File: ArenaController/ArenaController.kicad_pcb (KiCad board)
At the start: 2 copper layers, 63 x 112.3 mm, 30 parts, among them J1 RJ45, J2 RJ45, J4 RJ45, J5 RJ45, J6 RJ45, J7 Barrel_Jack, J8 Screw_Terminal_01x04, Q1 FS3400, Q2 FS3400, Q3 FS3400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

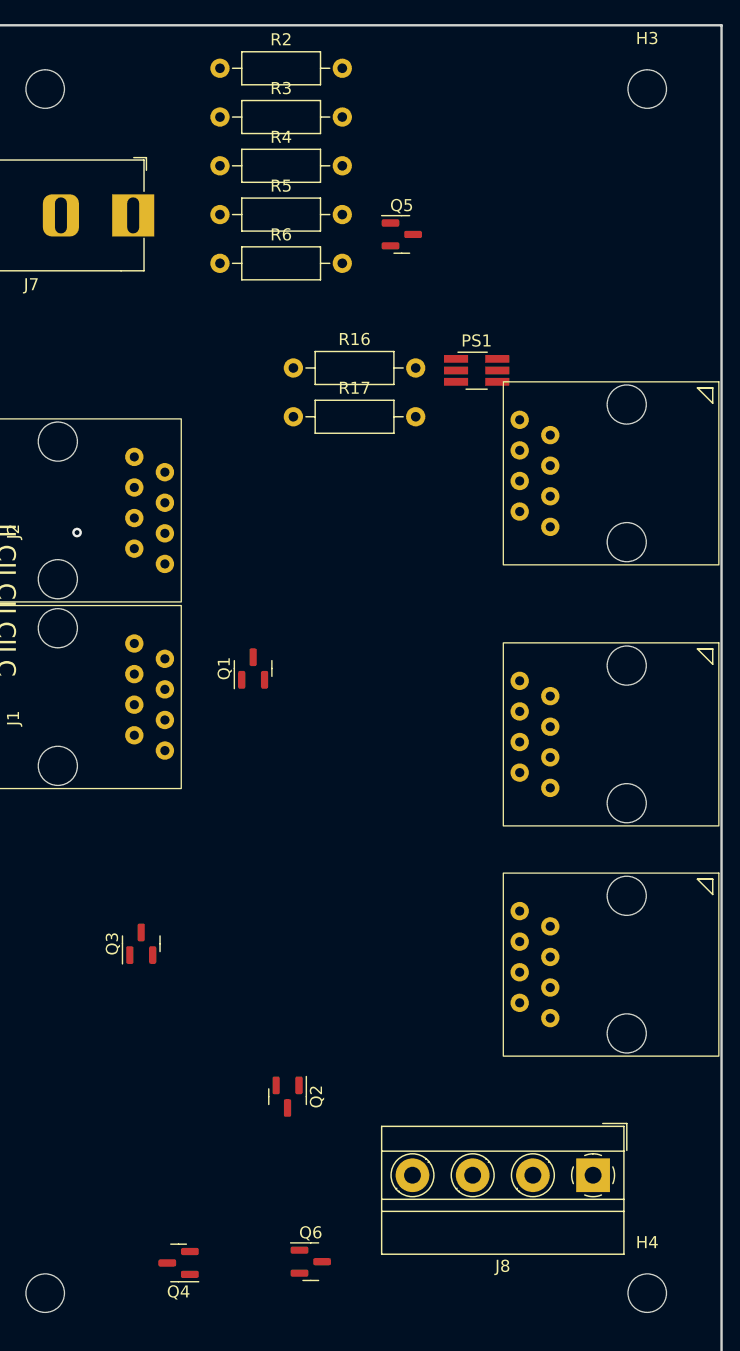
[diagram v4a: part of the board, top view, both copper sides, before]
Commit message: Added more SMD nightmare parts.
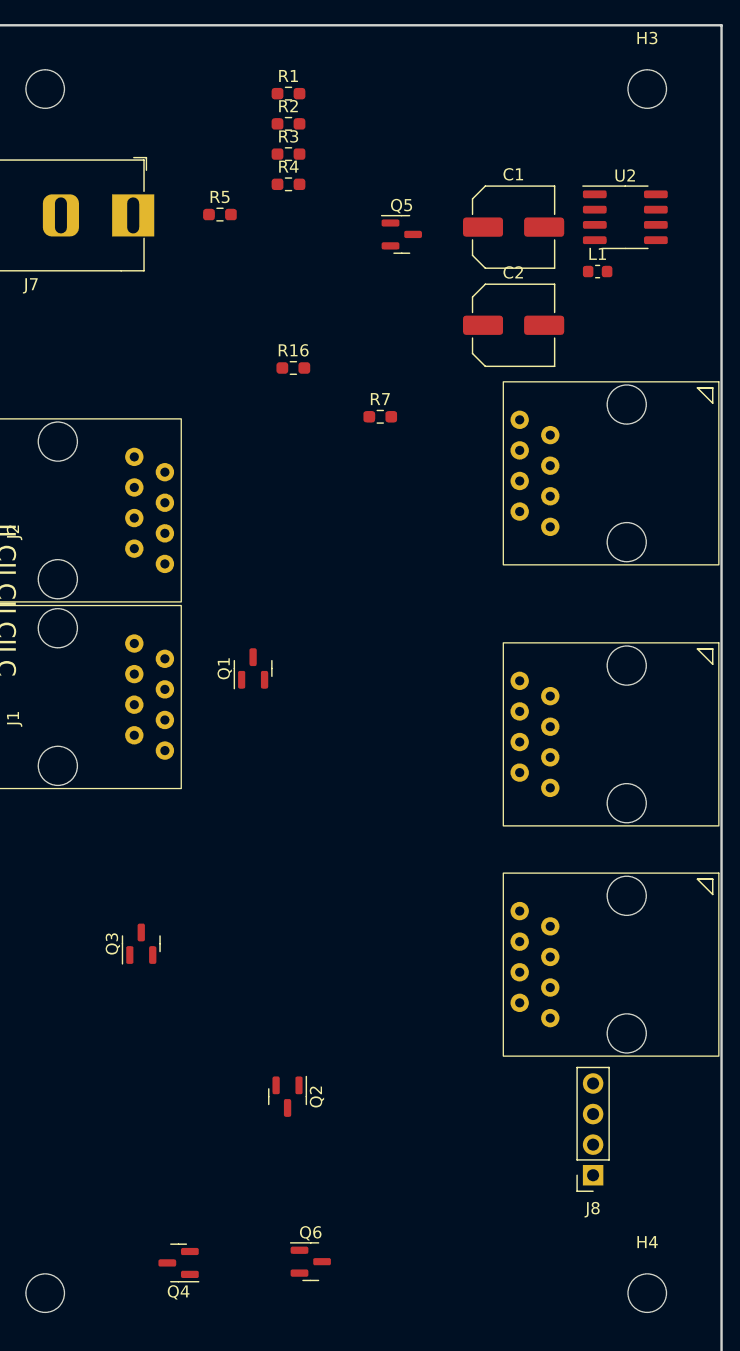
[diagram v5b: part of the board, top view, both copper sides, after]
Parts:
- removed PS1: ~, Package_TO_SOT_SMD:TSOT-23-6_HandSoldering
- removed R17: 10k, Resistor_THT:R_Axial_DIN0207_L6.3mm_D2.5mm_P10.16mm_Horizontal
- removed R6: 330, Resistor_THT:R_Axial_DIN0207_L6.3mm_D2.5mm_P10.16mm_Horizontal
- added C1: 100uF, Capacitor_SMD:C_Elec_6.3x5.4, F.Cu at (88.9, 61.5)
- added C2: 470uF, Capacitor_SMD:C_Elec_6.3x7.7, F.Cu at (88.9, 69.6)
- added L1: 47uH, Inductor_SMD:L_0603_1608Metric, F.Cu at (95.9, 65.2)
- added R1: 330, Resistor_SMD:R_0603_1608Metric_Pad0.98x0.95mm_HandSolder, F.Cu at (70.2, 50.4)
- added R7: 10k, Resistor_SMD:R_0603_1608Metric_Pad0.98x0.95mm_HandSolder, F.Cu at (77.8, 77.2)
- added U2: ~, Package_SO:SOP-8_3.76x4.96mm_P1.27mm, F.Cu at (98.2, 60.6)
- J8: footprint TerminalBlock_MetzConnect:TerminalBlock_MetzConnect_Type011_RT05504HBWC_1x04_P5.00mm_Horizontal -> Connector_PinSocket_2.54mm:PinSocket_1x04_P2.54mm_Vertical
- R16, R2, R3, R4, R5: footprint Resistor_THT:R_Axial_DIN0207_L6.3mm_D2.5mm_P10.16mm_Horizontal -> Resistor_SMD:R_0603_1608Metric_Pad0.98x0.95mm_HandSolder
- moved R2 7.33 mm to (70.2, 52.9)
- moved R3 6.47 mm to (70.2, 55.4)
- moved R4 5.90 mm to (70.2, 57.9)
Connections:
- R2 pad 1: Net-(Q1-G) -> Net-(Q3-G)
- R2 pad 2: /m_Green -> /m_Horn
- R3 pad 1: Net-(Q2-G) -> Net-(Q5-G)
- R3 pad 2: /m_Red_1 -> /m_Red_2
- R4 pad 1: Net-(Q3-G) -> Net-(Q2-G)
- R4 pad 2: /m_Horn -> /m_Red_1
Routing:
- net GND: vias 1 -> 0

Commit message: Swapped to ESP32 Devkit 4.
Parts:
- removed J7: Barrel_Jack, footprints:BarrelJack_Horizontal_TwoPin
- added J9: Barrel_Jack_MountingPin, Connector_BarrelJack:BarrelJack_Horizontal, F.Cu at (57.4, 64.5)
- added U3: ESP32-Devkit_C_V4, footprints:MODULE_ESP32_DEVKIT_C_V4, F.Cu at (19.3, 77.7)
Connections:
- L1 pad 1: Net-(U2-SW) -> Net-(L1-Pad1)
- U2 pad 5: (no net) -> Net-(L1-Pad1)
- U2 pad 6: (no net) -> Net-(L1-Pad1)
- U2 pad 7: (no net) -> GND
- U2 pad 8: (no net) -> GND

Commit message: small boardwork cleanup to try and lay it out.
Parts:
- removed kibuzzard-638A2138: G***, kibuzzard-638A2138
- removed kibuzzard-638A214B: G***, kibuzzard-638A214B
- removed kibuzzard-638A2165: G***, kibuzzard-638A2165
- removed kibuzzard-638A2178: G***, kibuzzard-638A2178
- moved J1 143.1 mm to (180.6, 67.2), turned to -90 degrees
- moved R1 72.4 mm to (131.2, 89.4)
- moved R2 72.4 mm to (131.2, 91.9)
- moved R3 72.4 mm to (131.2, 94.4)
- moved R4 72.4 mm to (131.2, 96.9)
- moved J4 61.5 mm to (122.8, 155.2), turned to 180 degrees
- moved Q4 60.6 mm to (115.8, 121.4)
- moved J9 53.1 mm to (110.2, 58.8), turned to -90 degrees
- moved L1 52.9 mm to (148.2, 57.5)
- moved R16 52.9 mm to (122.9, 65.5)
- moved Q3 52.9 mm to (110.3, 113.4)
- moved J6 52.9 mm to (158.3, 66.7)
- moved J8 52.9 mm to (147.8, 132.6)
- moved Q1 52.9 mm to (119.6, 90.5)
- moved Q2 52.9 mm to (122.5, 126.1)
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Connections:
- J4 pad 5: /G_Pause -> unconnected-(J4-Pad5)
- J4 pad 6: /G_End -> unconnected-(J4-Pad6)
- J4 pad 7: /G_Reset -> /G_End
- U2 pad 2: (no net) -> unconnected-(U2-NC-Pad2)
- U3 pad 11: /G_Reset -> unconnected-(U3-GPIO18/V_SPI_CLK/SCK-Pad11)
- U3 pad 25: /G_Pause -> unconnected-(U3-RTC_GPIO5/ADC1_7/GPIO35-Pad25)
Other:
- board size 63 x 112.3 mm -> 60 x 110 mm
- board text added: "Button 1"
- board text added: "Button 2"
- board text added: "Stacklight 1"
- board text added: "Stacklight 2"

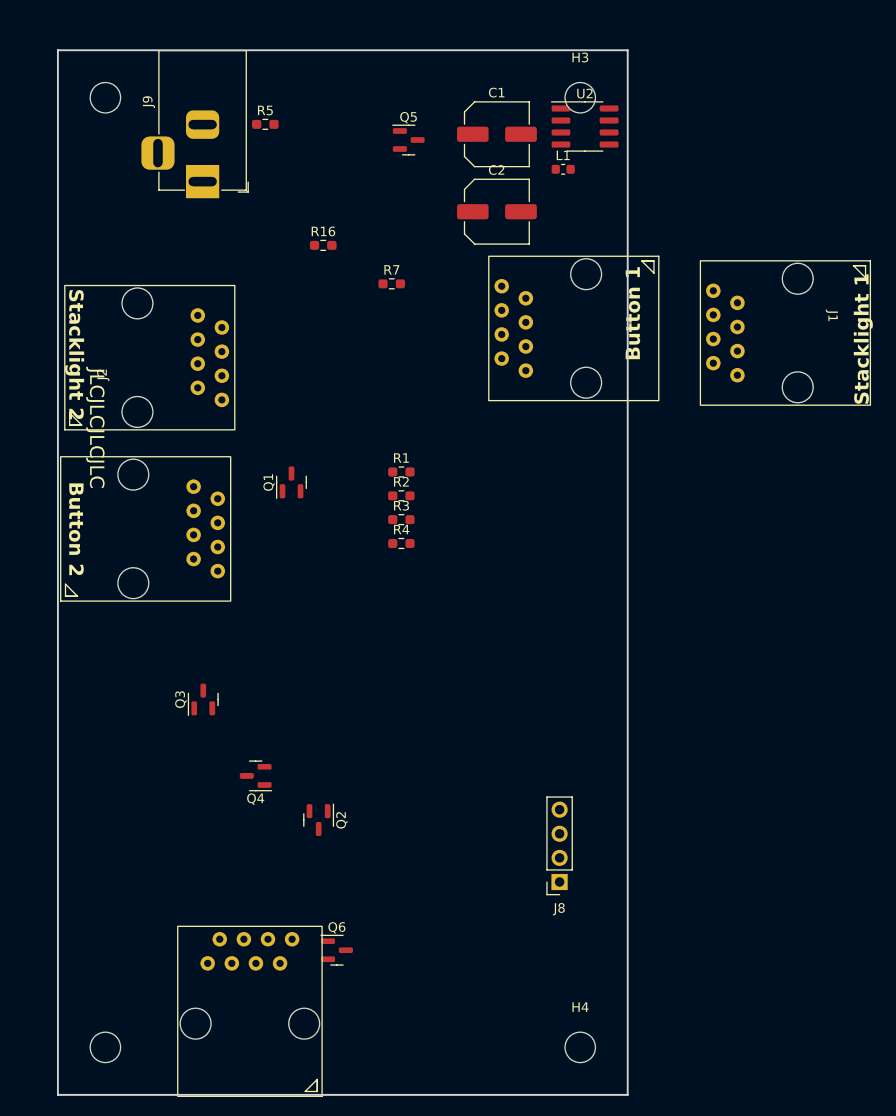
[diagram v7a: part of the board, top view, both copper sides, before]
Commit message: Started to organize board proper, did filled areas for 12V->5V input section.
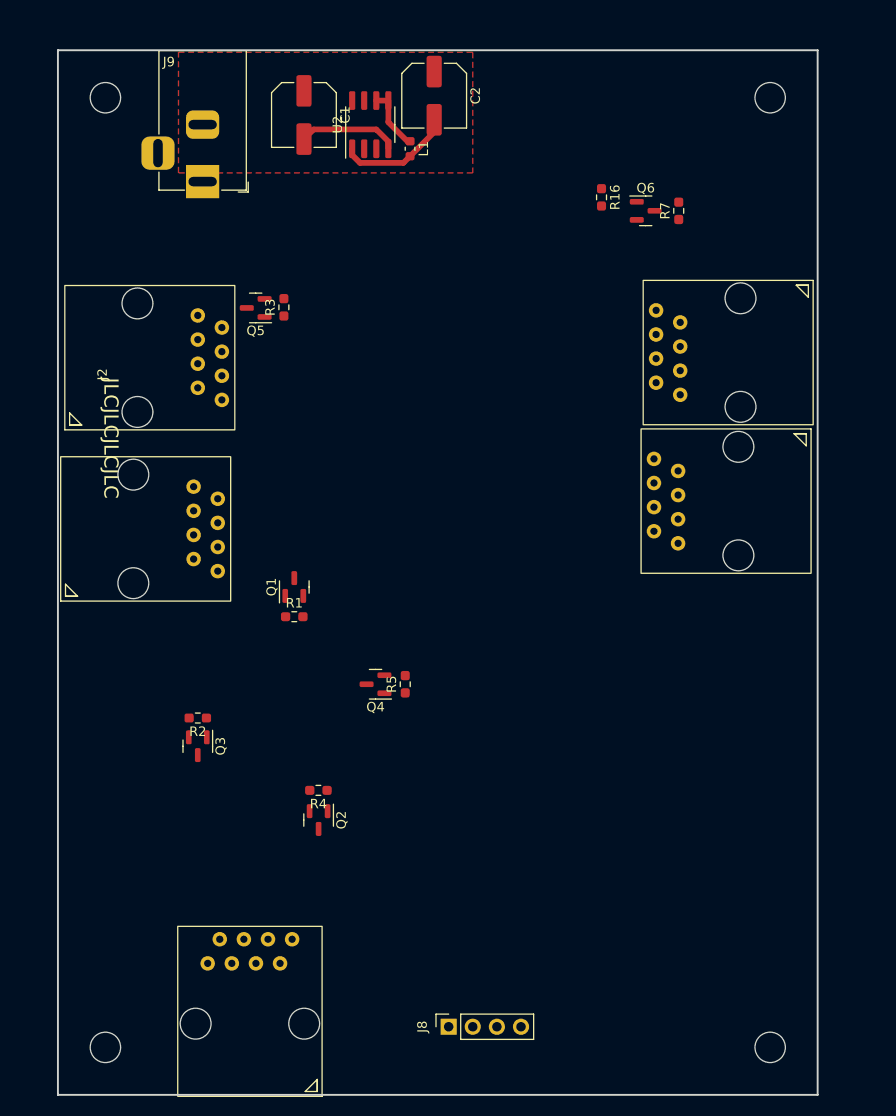
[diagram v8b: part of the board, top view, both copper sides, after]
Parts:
- moved Q6 84.4 mm to (156.9, 61.9)
- moved R5 60.8 mm to (131.6, 111.8), turned to 90 degrees
- moved R2 31.7 mm to (109.7, 115.3), turned to 180 degrees
- moved R7 31.2 mm to (160.4, 61.9), turned to 90 degrees
- moved R16 29.7 mm to (152.2, 60.5), turned to -90 degrees
- moved R4 27.4 mm to (122.4, 122.9), turned to 180 degrees
- moved R3 25.6 mm to (118.8, 72.1), turned to 90 degrees
- moved Q5 23.9 mm to (115.8, 72.1), turned to 180 degrees
- moved U2 22.6 mm to (127.9, 52.8), turned to 90 degrees
- moved C1 20.4 mm to (120.9, 51.8), turned to -90 degrees
- moved H3 20.0 mm to (170.0, 50.0)
- moved H4 20.0 mm to (170.0, 150.0)
- moved J8 19.2 mm to (136.1, 147.8), turned to 90 degrees
- moved R1 19.0 mm to (119.9, 104.6)
- moved J1 18.8 mm to (174.3, 84.9)
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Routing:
- net +5V: track 0.00 -> 12.3 mm
- net +12V: track 0.00 -> 10.6 mm
- net Net-(L1-Pad1): track 0.00 -> 6.67 mm
- added copper zone on F.Cu, net GND
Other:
- board size 60 x 110 mm -> 80 x 110 mm
